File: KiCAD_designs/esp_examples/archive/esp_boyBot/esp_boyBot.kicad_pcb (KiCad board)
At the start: 2 copper layers, 74.5 x 72 mm, 32 parts, among them J1 B4B-ZR-SM4-TFT_LF__SN_, J2 B2B-PH-SM4-TBLFSN, J3 Conn_01x02_Pin, J4 B4B-ZR-SM4-TFT_LF__SN_, J5 Conn_01x02_Pin, J6 B7B-ZR-SM4-TFT_LF__SN_, SW1 D2FS-FL-N-A, SW2 RS-282G05A3-SM RT, SW3 RS-282G05A3-SM RT, SW4 D2FS-FL-N-A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

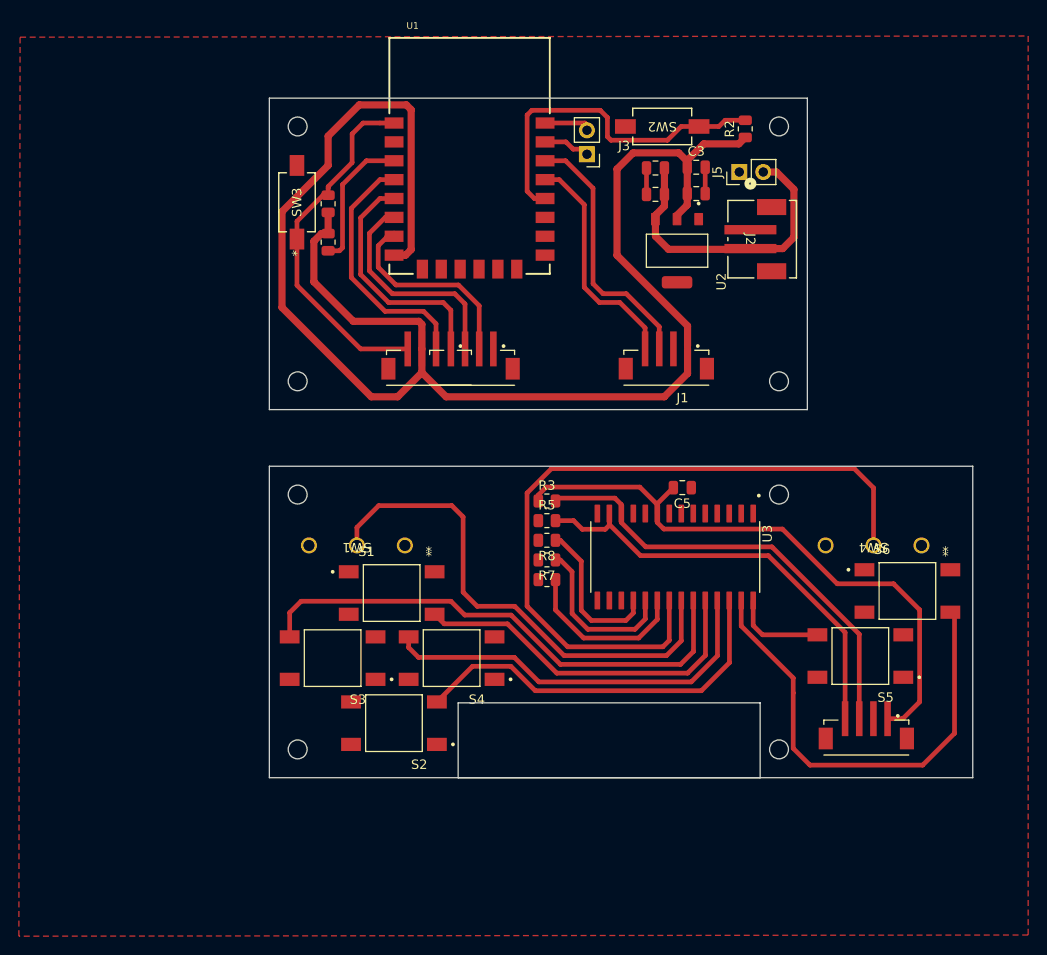
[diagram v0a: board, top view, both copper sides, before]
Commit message: UI mistake cam_roller
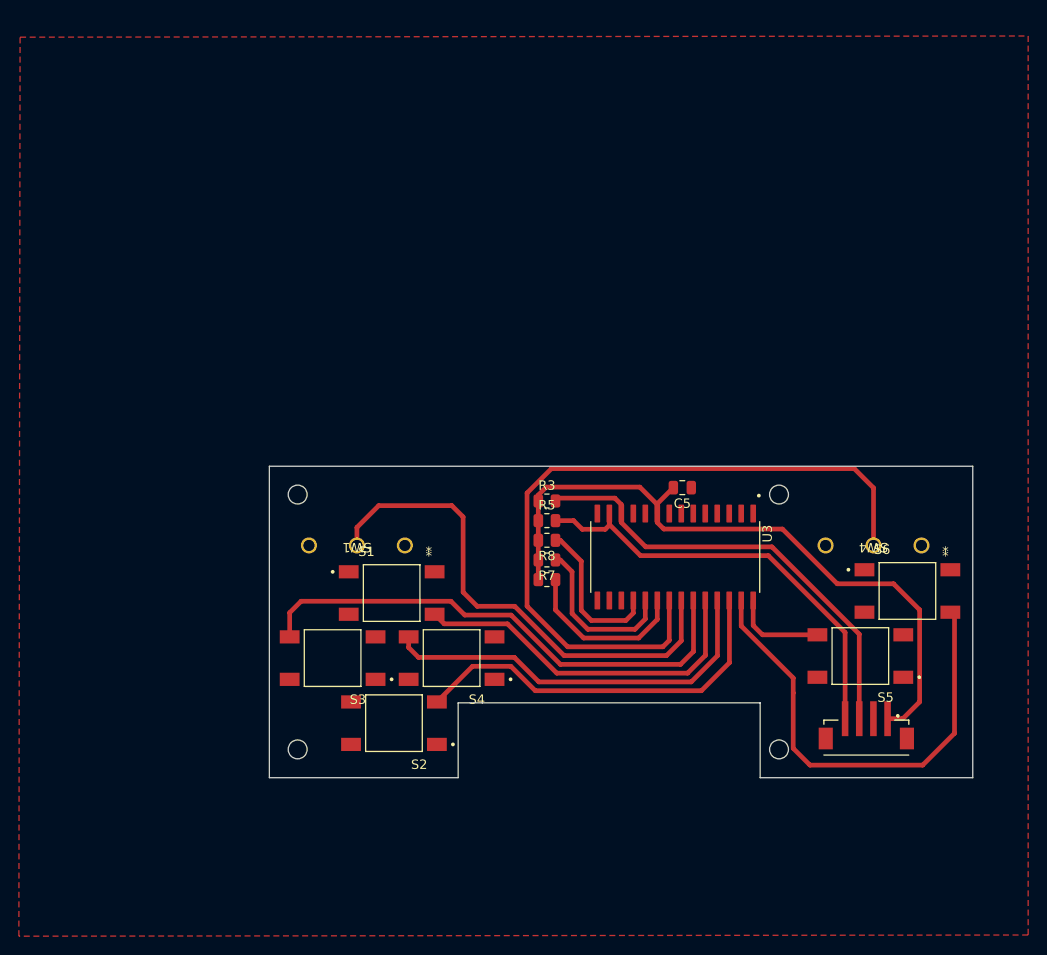
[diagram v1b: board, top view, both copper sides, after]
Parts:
- removed C1, C2, C3, C4: C, Capacitor_SMD:C_0805_2012Metric
- removed J1: B4B-ZR-SM4-TFT_LF__SN_, esp_lib:JST_B4B-ZR-SM4-TFT_LF__SN_
- removed J2: B2B-PH-SM4-TBLFSN, esp_lib:B2B-PH-SM4-TBLFSN_JST
- removed J3, J5: Conn_01x02_Pin, Connector_PinHeader_2.54mm:PinHeader_1x02_P2.54mm_Vertical
- removed J6: B7B-ZR-SM4-TFT_LF__SN_, esp_lib:B7B-ZR-SM4-TBLFSN_JST
- removed R1, R2, R4: R, Resistor_SMD:R_0805_2012Metric
- removed SW2, SW3: RS-282G05A3-SM RT, esp_lib:RS-282G05A3-SM RT_CNK
- removed U1: ESP-12F, esp_lib:ESP-12F
- removed U2: AMS1117-3.3, esp_lib:SOT229P700X180-4N
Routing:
- net VCC: track 237.1 -> 73.5 mm
- net /RST: track 38.2 -> 0.00 mm
- net /boot: track 37.0 -> 0.00 mm
- net /VIN: track 32.5 -> 0.00 mm
- net /SCK_mcp: track 76.0 -> 48.3 mm
- net /AO: track 26.5 -> 0.00 mm
- net /SDA_screen: track 25.3 -> 0.00 mm
- net /SDA_mcp: track 72.3 -> 47.5 mm
- net /CS: track 23.3 -> 0.00 mm
- net /SCK_screen: track 21.8 -> 0.00 mm
- net Net-(U1-EN): track 14.9 -> 0.00 mm
- net GND: track 5.59 -> 0.00 mm
- net Net-(J3-Pin_2): track 4.86 -> 0.00 mm
- net Net-(J3-Pin_1): track 4.76 -> 0.00 mm
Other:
- board size 74.5 x 72 mm -> 74.5 x 33 mm
